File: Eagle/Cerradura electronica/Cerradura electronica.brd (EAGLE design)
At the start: 65 x 50 mm, 19 parts, among them K1 G5L, M1 ARDUINO-NANO-3.0#ISP

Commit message: Completado SCH del nuevo Hardware al 50%
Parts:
- removed D1: 1N4004, adafruit:DO41-10
- removed K1: G5L, relay:G5LE
- removed LED1: verde, led:LED3MM
- removed M1: ARDUINO-NANO-3.0#ISP, DIY- comercial modules:ARDUINO-NANO-3.0#ISP
- removed OK1: PC817, optocoupler:DIL04
- removed R2: 10k, rcl:0204/7
- removed TECLADO: (no value), con-lstb:MA05-1
- removed X1: (no value), con-ptr500:AK500/3
- added C6, C7, C8, C9: 0.1u, rcl:C0805
- added ISP: (no value), con-lstb:MA03-2
- added L1: 10u, Circuitos-Creativos-RCL:L0805
- added SV1: (no value), con-lstb:MA04-1
- added U1: ATMEGA328P_TQFP, SparkFun-DigitalIC:TQFP32-08
- added XT2: 8MHz, crystal:CTS406
- C1, C2: value 100n -> 22pF; device rcl:C025-025X050 -> rcl:C0805
- C3, C4: value 100n -> 0.1uF; device rcl:C025-025X050 -> rcl:C0805
- C5: value 100n -> 1uF; device rcl:C025-025X050 -> rcl:C0805
- R1, R3, R4: device rcl:0204/7 -> rcl:R1206
- R5, R6: value 1k -> 10k; device rcl:0204/7 -> rcl:R1206
- U$1: value A5_HORIZONTAL -> A4_HORIZONTAL
- moved C5 79.1 mm to (0.50, -34.5), turned to 0 degrees
- moved U$1 76.7 mm to (-12.0, -32.5)
- moved R1 64.4 mm to (-4.00, -34.5), turned to 0 degrees
- moved C4 63.1 mm to (2.00, -28.0), turned to 0 degrees
- moved C3 59.8 mm to (-4.50, -28.0), turned to 0 degrees
- moved C2 55.8 mm to (14.5, -28.0), turned to 0 degrees
- moved C1 50.6 mm to (8.50, -28.0), turned to 0 degrees
- moved R6 33.3 mm to (5.00, 21.5), turned to 180 degrees
- moved R5 30.8 mm to (5.00, 15.5), turned to 180 degrees
- moved R4 26.1 mm to (5.00, 33.5), turned to 180 degrees
- moved R3 21.1 mm to (5.00, 27.5), turned to 180 degrees
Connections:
- removed net +12V: C5.1, D1.C, K1.1, M1.J2.1, X1.1
- removed net +5V: M1.J2.4, TECLADO.5
- removed net 1A: C3.1, M1.J1.9, R3.1, TECLADO.2
- removed net 2B: C4.1, M1.J1.8, R4.1, TECLADO.1
- removed net 3C: C1.1, M1.J1.11, R1.1, TECLADO.4
- removed net 3V3: M1.J2.14
- removed net 4D: C2.1, M1.J1.10, R2.1, TECLADO.3
- removed net GND.2: M1.J2.2
- removed net N$1: LED1.A, R6.2
- removed net N$2: C5.2, D1.A, K1.2, OK1.4
- removed net N$3: OK1.1, R5.2
- removed net N$4: K1.S, X1.3
- removed net RELE: M1.J1.6, R5.1, R6.1
- new net A0: U1.23
- new net A1: U1.24
- new net A2: U1.25
- new net A3: U1.26
- new net A6: U1.19
- new net A7: U1.22
- new net AREF: C4.1, U1.20
- new net AVCC: C5.1, L1.2, U1.18
- new net D10: U1.14
- new net D2: U1.32
- new net D3: U1.1
- new net D4: U1.2
- new net D5/2: C7.1, R4.1, U1.9
- new net D6/1: C6.1, R3.1, U1.10
- new net D7/4: C9.1, R6.1, U1.11
- new net D8/3: C8.1, R5.1, U1.12
- new net D9: U1.13
- new net MISO: ISP.4, U1.16
- new net MOSI: ISP.6, U1.15
- new net OS1: C1.1, U1.7, XT2.3
- new net OS2: C2.1, U1.8, XT2.1
- new net RST: ISP.3, R1.2, U1.29
- new net RX1: SV1.3, U1.30
- new net SCK: ISP.2, U1.17
- new net TX0: SV1.2, U1.31
- new net VCC: C3.1, ISP.5, L1.1, R1.1, SV1.1, U1.4, U1.6
- net GND: now also C5.2, C6.2, C7.2, C8.2, C9.2, ISP.1, R5.2, R6.2, SV1.4, U1.21, U1.3, U1.5; no longer K1.P, LED1.K, M1.J1.4, OK1.2, OK1.3, R1.2, R2.2, X1.2
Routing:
- net GND: track 134.2 -> 0.00 mm
- net +12V: track 102.1 -> 0.00 mm
- net +5V: track 57.3 -> 0.00 mm
- net 2B: track 37.3 -> 0.00 mm
- net N$2: track 34.7 -> 0.00 mm
- net 1A: track 29.2 -> 0.00 mm
- net 4D: track 24.0 -> 0.00 mm
- net N$3: track 21.5 -> 0.00 mm
- net N$4: track 20.1 -> 0.00 mm
- net 3C: track 19.2 -> 0.00 mm
- net RELE: track 9.46 -> 0.00 mm
- net N$1: track 5.89 -> 0.00 mm
- removed copper zone on layer 16, net GND

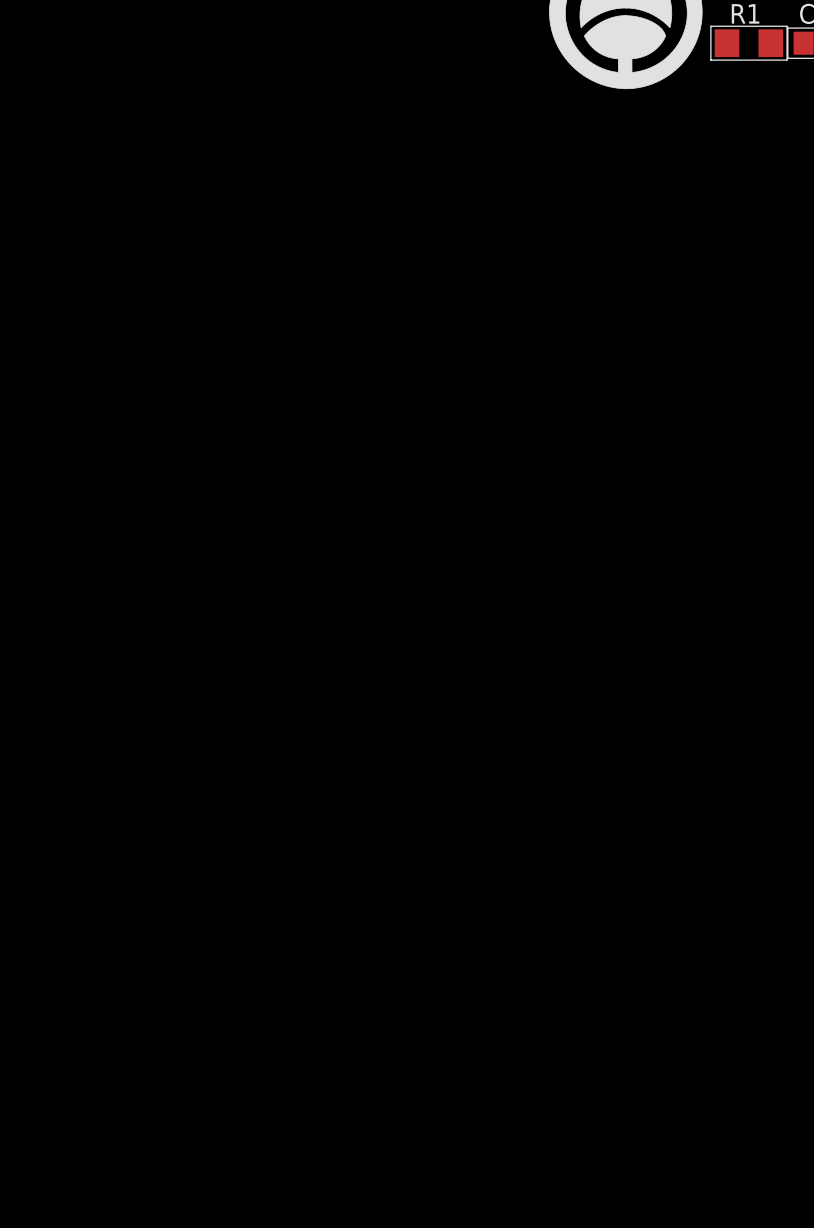
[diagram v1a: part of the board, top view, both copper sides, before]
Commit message: Terminado regulador 5V y etapa de potencia
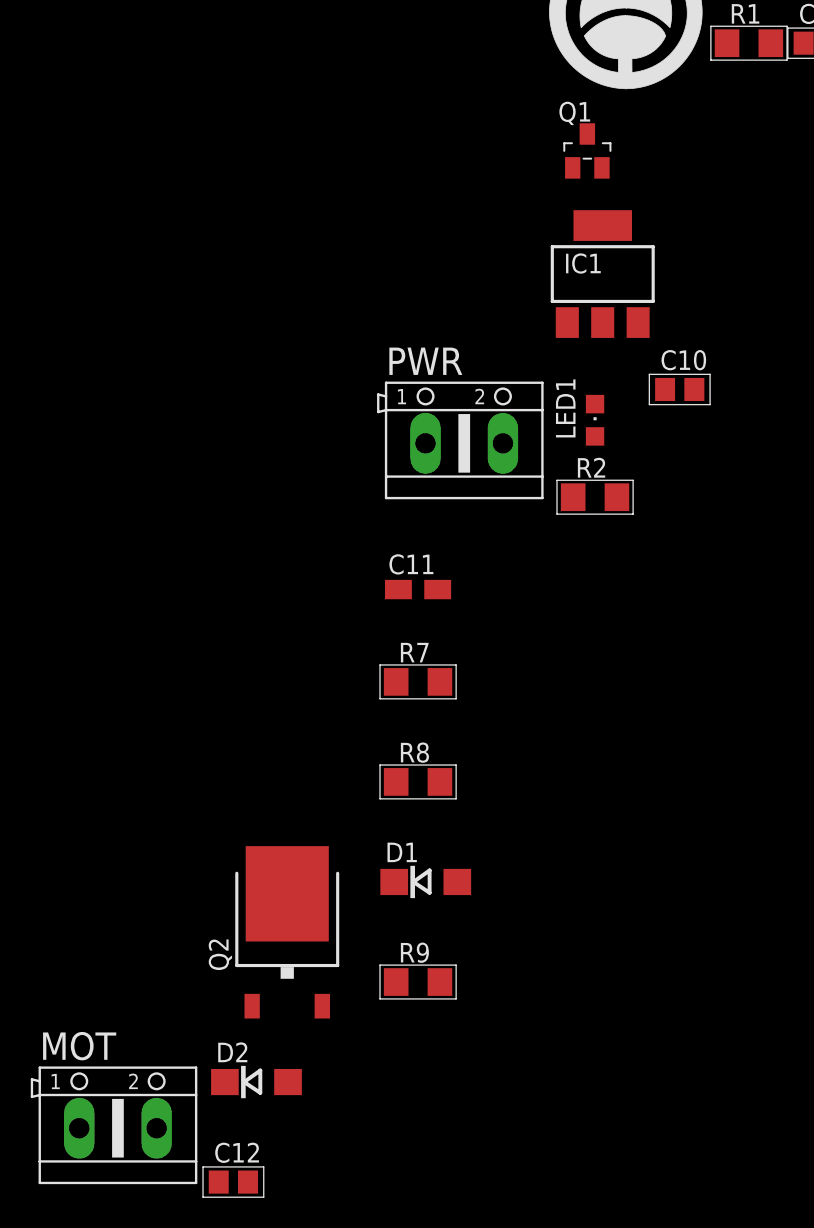
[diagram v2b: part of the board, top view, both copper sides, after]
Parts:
- added C10: 10uF, rcl:C0805
- added C11: 47uF, rcl:R/2012-12W
- added C12: 0.1u, rcl:C0805
- added D1, D2: 4004, diode:DO214AC
- added IC1: LD117AS50TR, v-reg:SOT223
- added LED1: Green, led:CHIPLED_0805
- added MOT, PWR: (no value), con-ptr500:AK500/2
- added Q1: 2N3904, transistor:SOT23-BEC
- added Q2: IRF540NS, Circuitos-Creativos-Transistores:TO-252
- added R2, R7: 1k, rcl:R1206
- added R8, R9: 10k, rcl:R1206
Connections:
- new net +12V: C10.1, C12.1, D1.A, D2.C, MOT.1, PWR.1, R9.1
- new net N$1: LED1.A, R2.2
- new net N$2: Q1.B, R7.2, R8.2
- new net N$3: D1.C, IC1.3
- new net N$4: Q1.C, Q2.1, R9.2
- new net N$5: C12.2, D2.A, MOT.2, Q2.3
- net D3: now also R7.1
- net GND: now also C10.2, C11.-, IC1.1, LED1.C, PWR.2, Q1.E, Q2.2
- net VCC: now also C11.+, IC1.4, R2.1, R8.1

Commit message: Terminado el SCH, inicio del BRD
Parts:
- added R10: 10k, rcl:R1206
- added S1: Reset, Testing:TACTILE-SWITCH-1101NE
- added TECLADO: (no value), con-lstb:MA07-1
- moved C1 138.4 mm to (116.5, 58.5)
- moved C10 138.4 mm to (99.5, 29.5)
- moved C11 138.4 mm to (82.5, 16.5)
- moved C12 138.4 mm to (70.5, -22.0)
- moved C2 138.4 mm to (122.5, 58.5)
- moved C3 138.4 mm to (103.5, 58.5)
- moved C4 138.4 mm to (110.0, 58.5)
- moved C5 138.4 mm to (108.5, 52.0)
- moved D1 138.4 mm to (83.0, -2.50)
- moved D2 138.4 mm to (72.0, -15.5)
- moved IC1 138.4 mm to (94.5, 37.0)
- moved ISP 138.4 mm to (105.5, 66.5)
- moved L1 138.4 mm to (113.5, 52.0)
- moved LED1 138.4 mm to (94.0, 27.5)
- moved MOT 138.4 mm to (63.0, -18.5)
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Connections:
- removed net N$5: C12.2, D2.A, MOT.2, Q2.3
- new net MOT_ON: C12.2, D2.A, MOT.2, Q2.3, TECLADO.2
- new net N$11: R10.2, TECLADO.1
- new net RESET: R1.2, S1.P$2, U1.29
- net +12V: now also R10.1
- net D5/2: now also TECLADO.7
- net D6/1: now also TECLADO.6
- net D7/4: now also TECLADO.5
- net D8/3: now also TECLADO.4
- net GND: now also S1.P$1
- net RST: no longer R1.2, U1.29
- net VCC: now also TECLADO.3

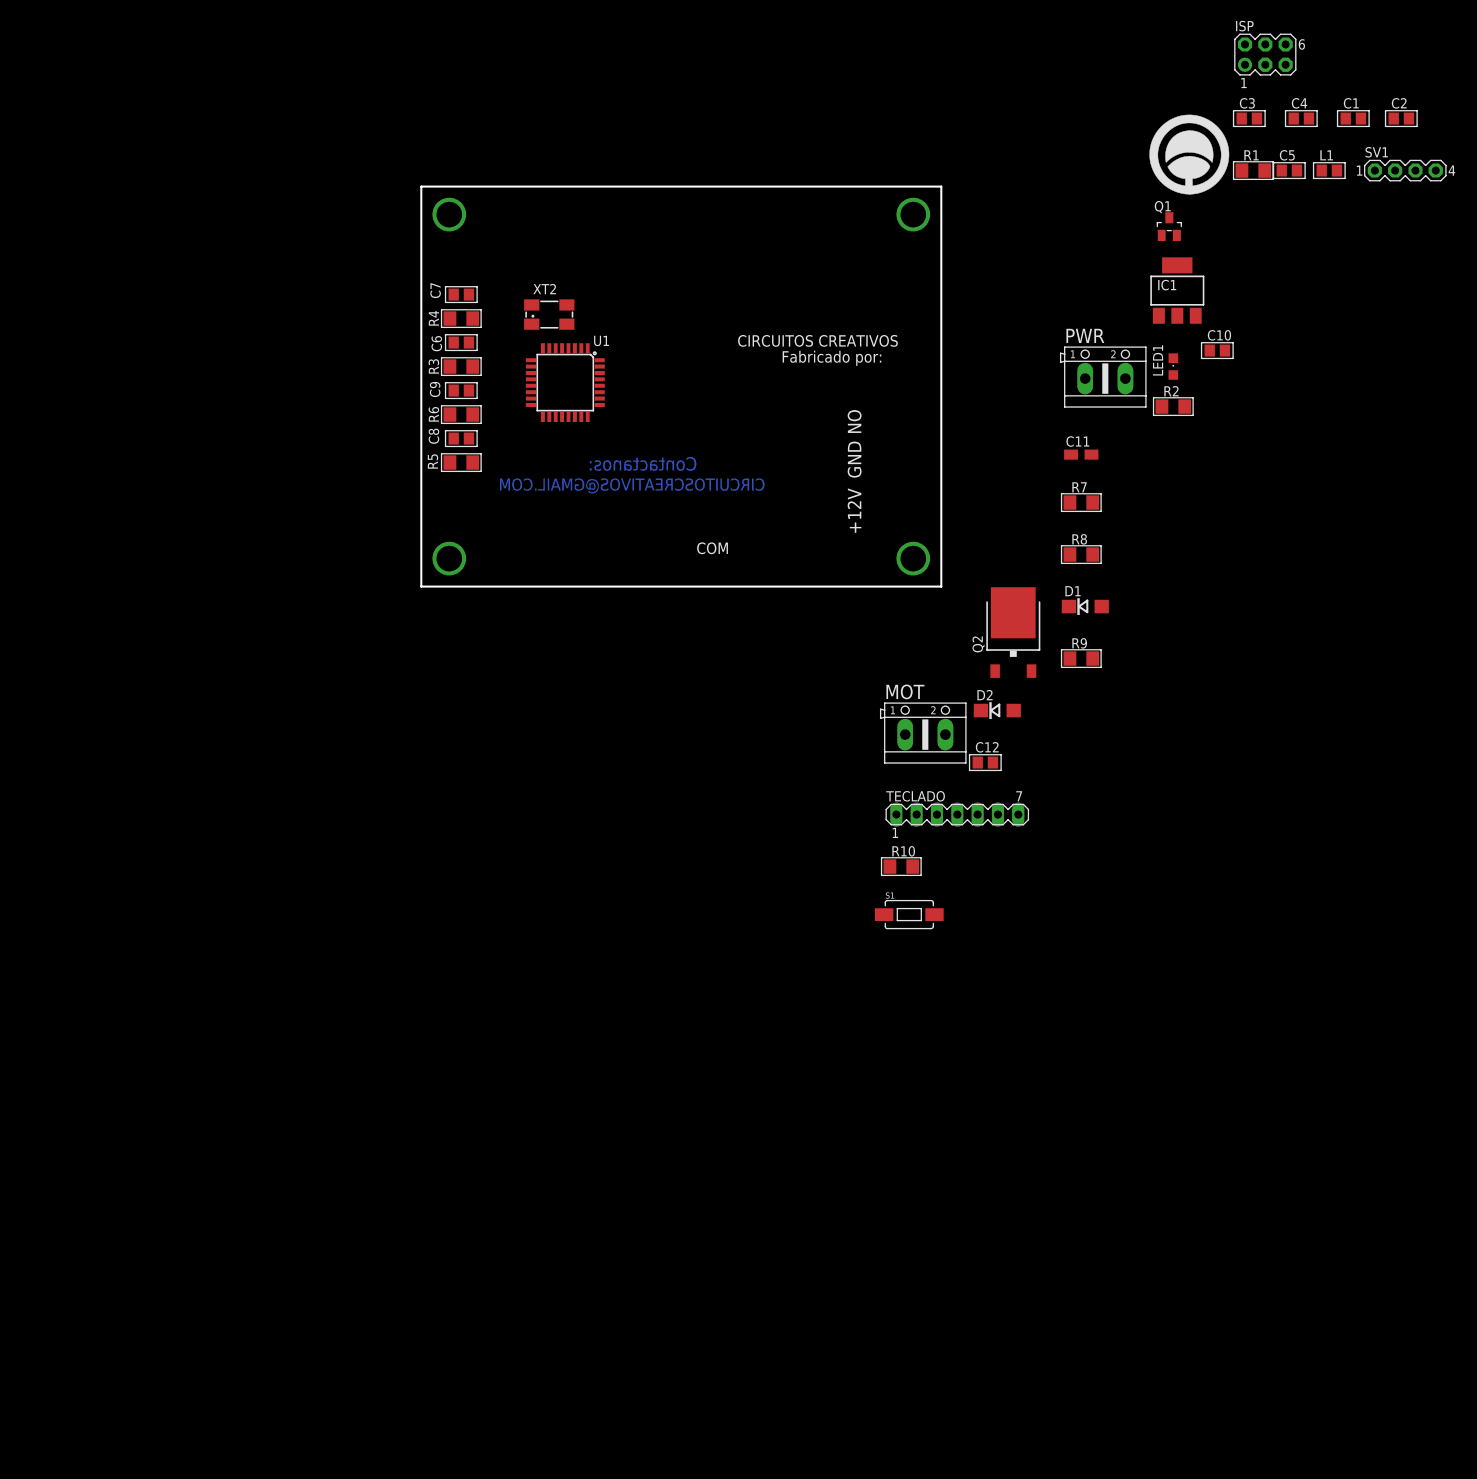
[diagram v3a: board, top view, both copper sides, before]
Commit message: Componentes ubicados, inicio ruteo
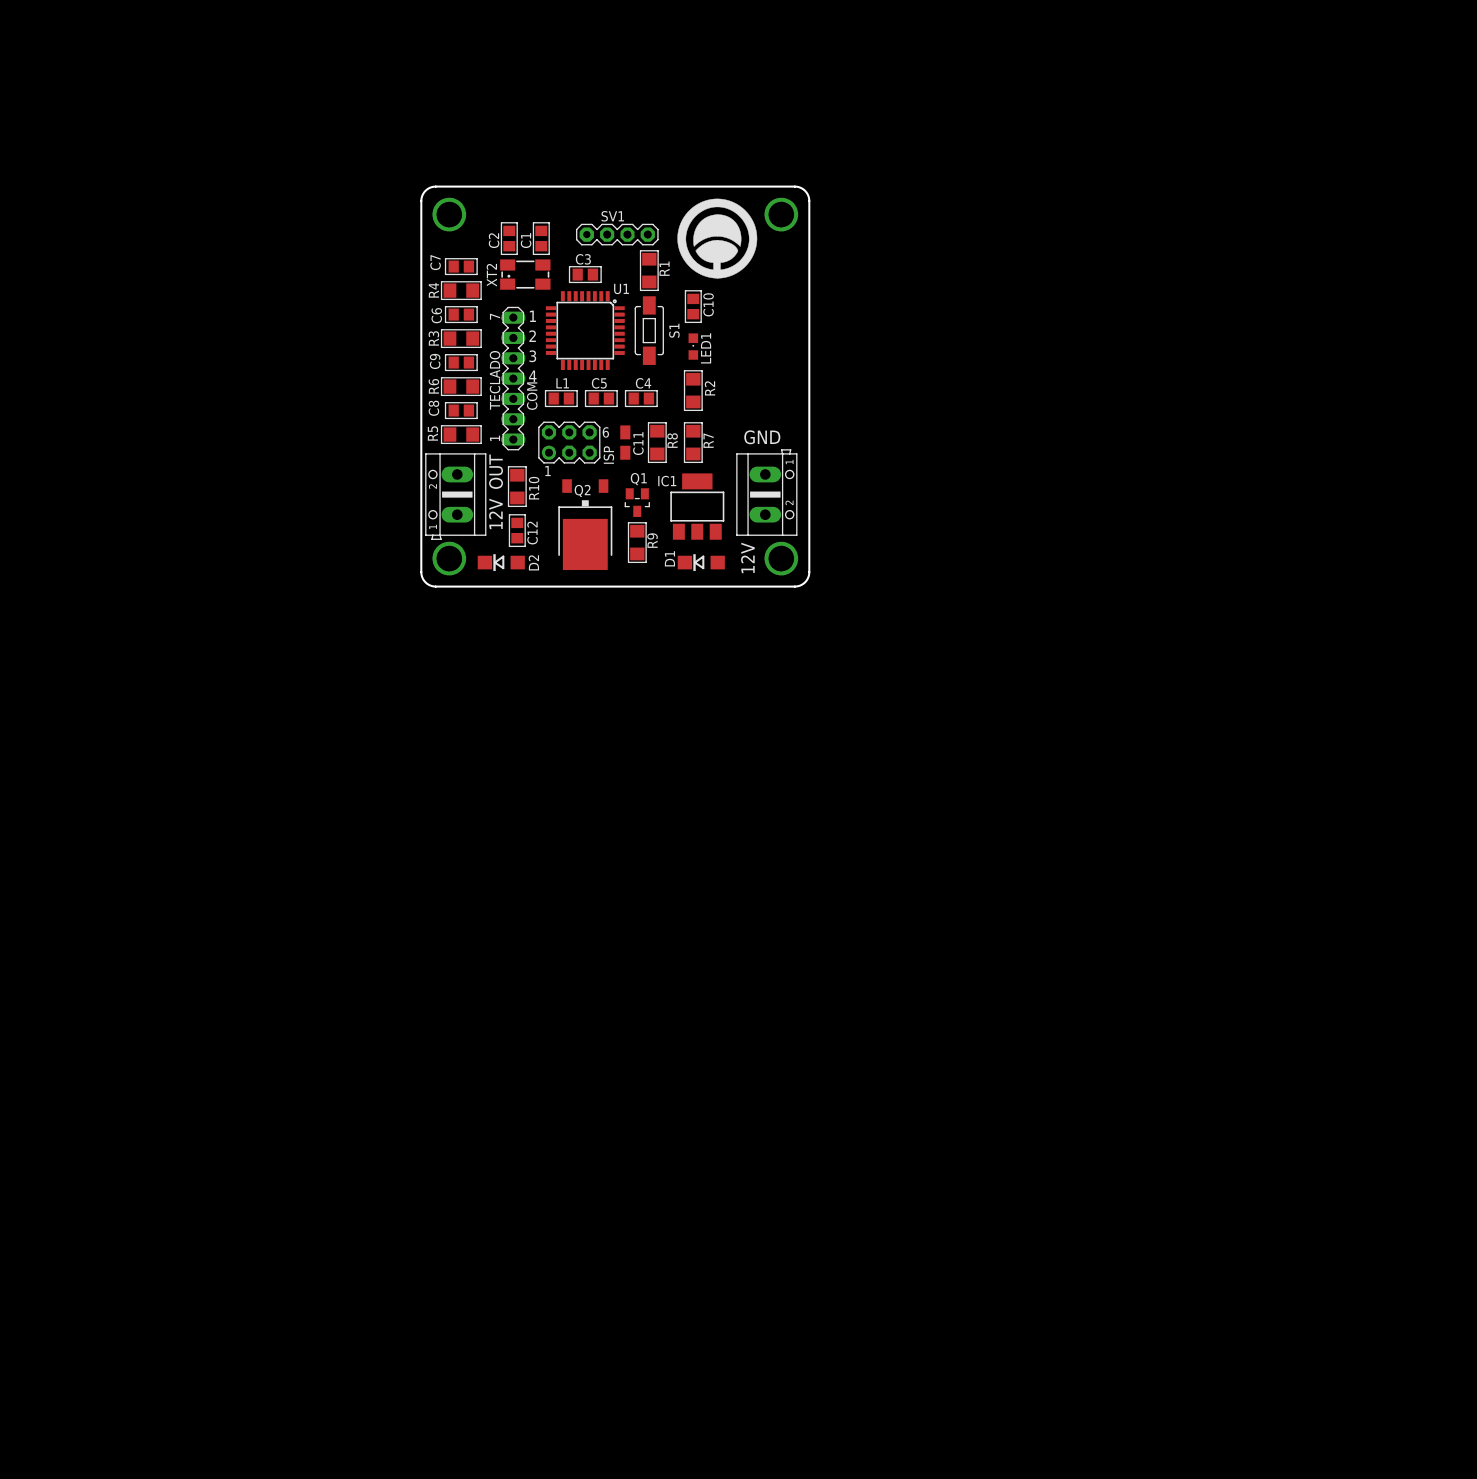
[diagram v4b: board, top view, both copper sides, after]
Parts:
- moved C2 112.5 mm to (11.0, 43.5), turned to 90 degrees
- moved C1 102.6 mm to (15.0, 43.5), turned to 90 degrees
- moved L1 100.1 mm to (17.5, 23.5)
- moved ISP 99.6 mm to (18.5, 18.0)
- moved SV1 98.8 mm to (24.5, 44.0)
- moved C5 90.6 mm to (22.5, 23.5)
- moved C4 89.6 mm to (27.5, 23.5)
- moved C3 85.3 mm to (20.5, 39.0)
- moved S1 79.9 mm to (28.5, 32.0), turned to 270 degrees
- moved TECLADO 77.8 mm to (11.5, 26.0), turned to 90 degrees
- moved R1 76.5 mm to (28.5, 39.5), turned to 270 degrees
- moved Q1 74.9 mm to (27.0, 10.5), turned to 180 degrees
- moved R10 67.5 mm to (12.0, 12.5), turned to 90 degrees
- moved IC1 65.8 mm to (34.5, 10.0)
- moved MOT 65.7 mm to (4.50, 11.5), turned to 90 degrees
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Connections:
- removed net RESET: R1.2, S1.P$2, U1.29
- net +12V: now also PWR.2; no longer PWR.1
- net GND: now also PWR.1; no longer PWR.2
- net RST: now also R1.2, S1.P$2, U1.29
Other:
- board size 65 x 50 mm -> 48.5 x 50 mm
- board text added: "1"
- board text added: "12V"
- board text added: "2"
- board text added: "3"
- board text added: "4"
- board text added: "OUT"
- board text removed: "+12V"
- board text removed: "CIRCUITOSCREATIVOS@GMAIL.COM"
- board text removed: "Contactanos:"
- board text removed: "NO"
